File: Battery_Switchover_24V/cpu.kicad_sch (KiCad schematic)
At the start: 42 parts, among them J8 USB_C_Receptacle_USB2.0_14P, SW1 SW_Push, U3 LPC11U14FBD48-201, U4 L5973D, U6 AMS1117-3.3, Y1 12.000MHz

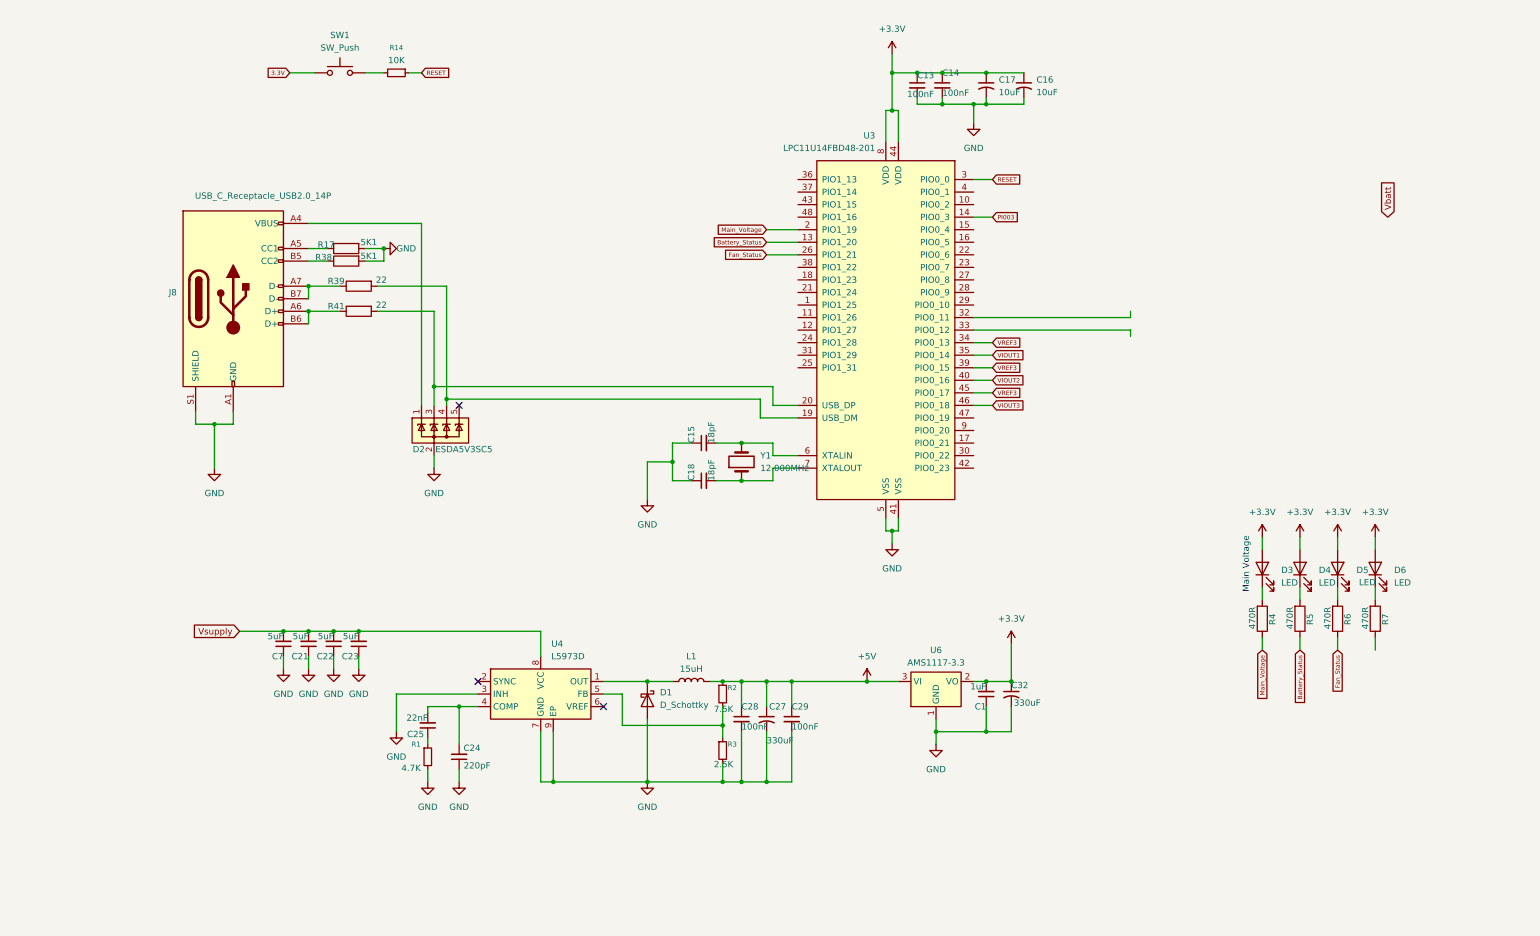
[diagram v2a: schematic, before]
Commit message: Added SCL and SDA from the tempreture sensor to the CPU
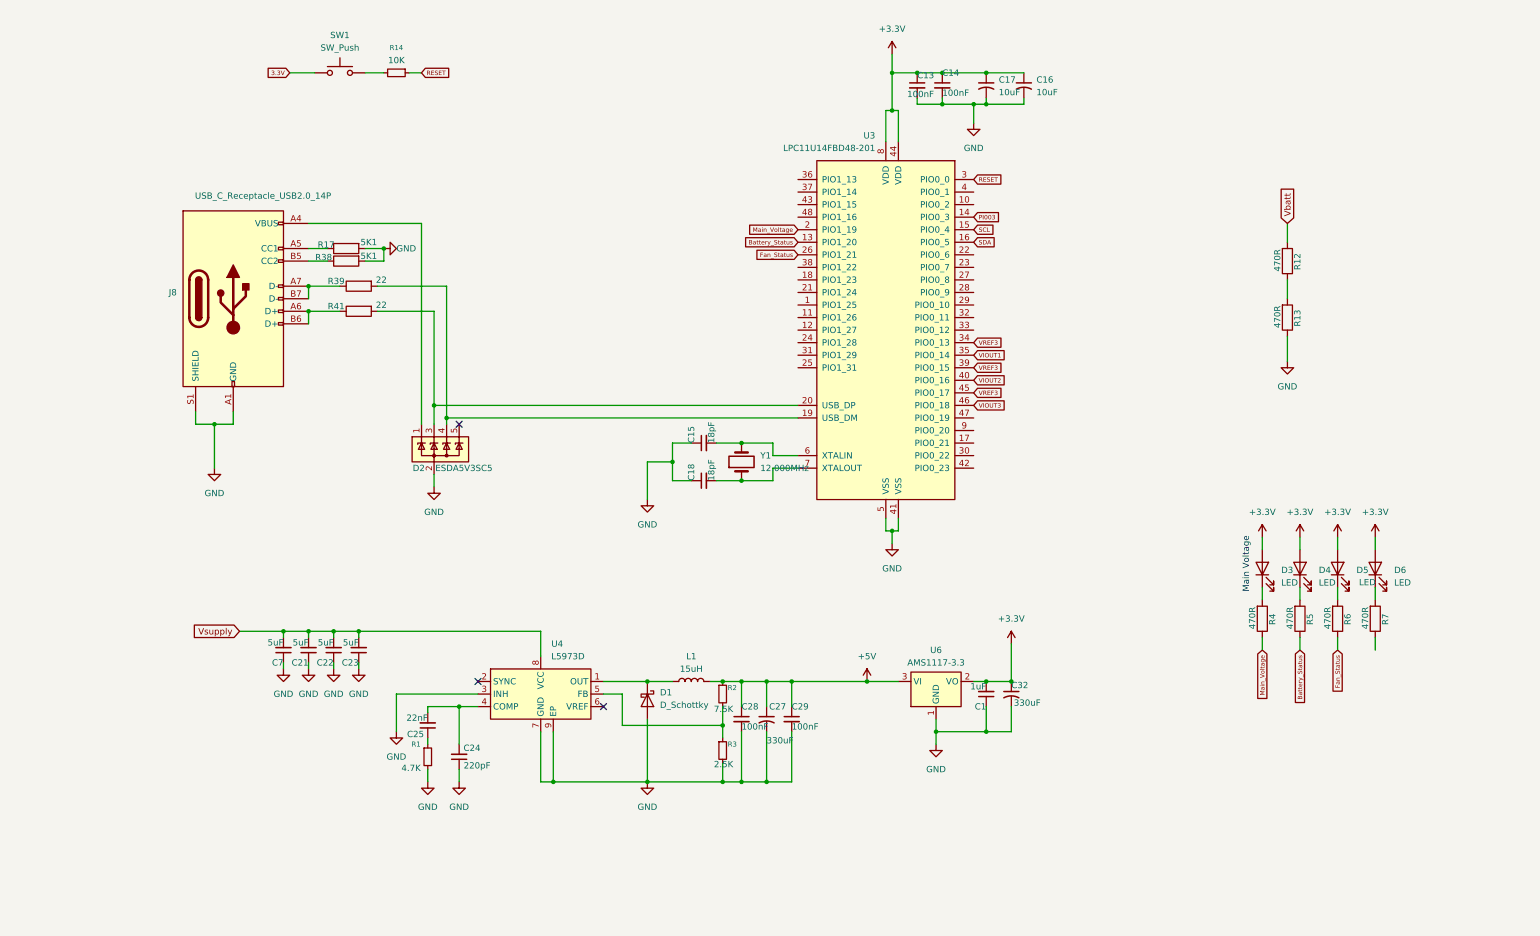
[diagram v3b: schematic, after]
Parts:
- added R12, R13: 470R, Resistor_SMD:R_0603_1608Metric, symbol Device:R
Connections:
- net GND: now also R13.1
- net Vbatt: now also R12.2
- net SCL: now reaches U3.15 (PIO0_4)
- net SDA: now reaches U3.16 (PIO0_5)
- new net: R12.1, R13.2
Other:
- moved on the sheet: C21, C22, C23, C7, D2

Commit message: Voltaj ölçümü eklendi Lm75 LM60 ile değiştirildi
LM75 LM60 ile değiştirildi Vin ve Vbattery voltaj ölçümü için TVS li voltaj bölücüler ADC ye bağlandı Vin 5V converter arasına TVS konuldu 5V converter giriş cap ları değiştirildi. Reset düğmesine debounce cap eklendi.
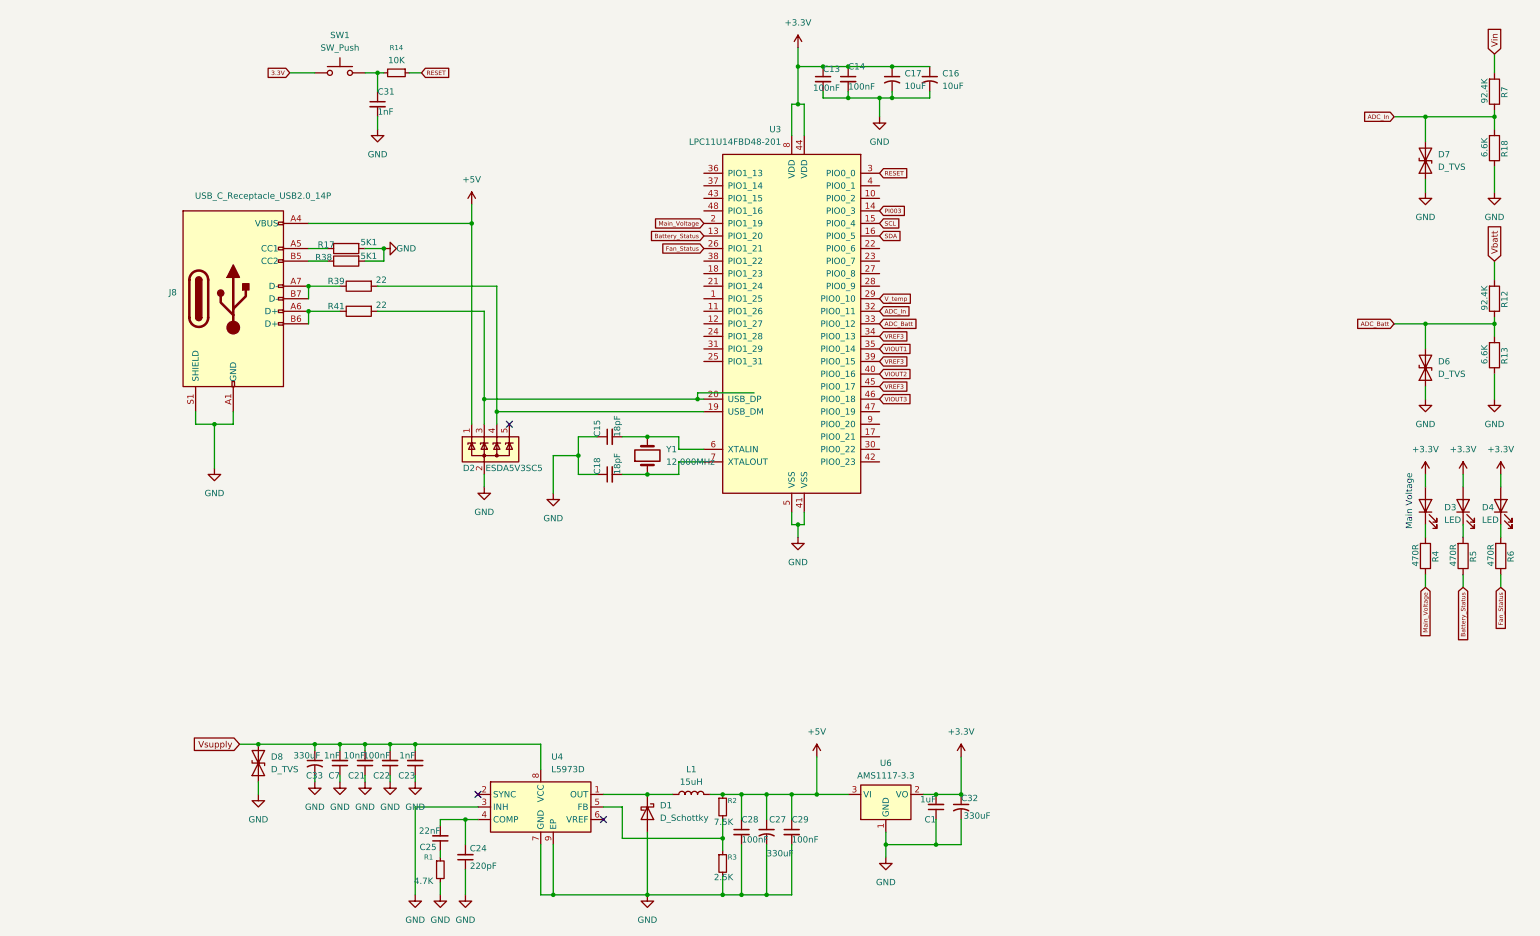
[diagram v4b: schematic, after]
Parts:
- removed D6: LED, symbol Device:LED
- added C31: 1nF, symbol Device:C_Small
- added C33: 330uF, symbol Device:C_Small_US
- added D6, D7, D8: D_TVS, symbol Device:D_TVS
- added R18: 6.6K, Resistor_SMD:R_0603_1608Metric, symbol Device:R
- C21: value 5uF -> 10nF
- C22: value 5uF -> 100nF
- C23, C7: value 5uF -> 1nF
- R12, R7: value 470R -> 92.4K
- R13: value 470R -> 6.6K
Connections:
- net +5V: now also D2.1 (K), J8.A4 (VBUS), J8.A9 (VBUS), J8.B4 (VBUS), J8.B9 (VBUS)
- net GND: now also C31.2, C33.2, D6.1 (A1), D7.1 (A1), D8.1 (A1), R18.1
- net Vsupply: now also C33.1, D8.2 (A2)
- net V_temp: now reaches U3.29 (PIO0_10)
- net ADC_In: now reaches U3.32 (PIO0_11)
- net ADC_In: now also R7.1, D7.2 (A2), R18.2
- net ADC_Batt: now reaches U3.33 (PIO0_12)
- net ADC_Batt: now also R12.1, R13.2, D6.2 (A2)
- net Vin: now reaches R7.2
- net at R14.2, SW1.2: now also C31.1
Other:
- moved on the sheet: C1, C13, C14, C15, C16, C17, C18, C21, C22, C23, C24, C25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

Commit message: Added Some Protection MEasures and redid the Fan Contrlll
Added TVS diodes battery monitor inputs and outputs and some capacitors added fan controll fixed output capacitances of battery monitoring circuit
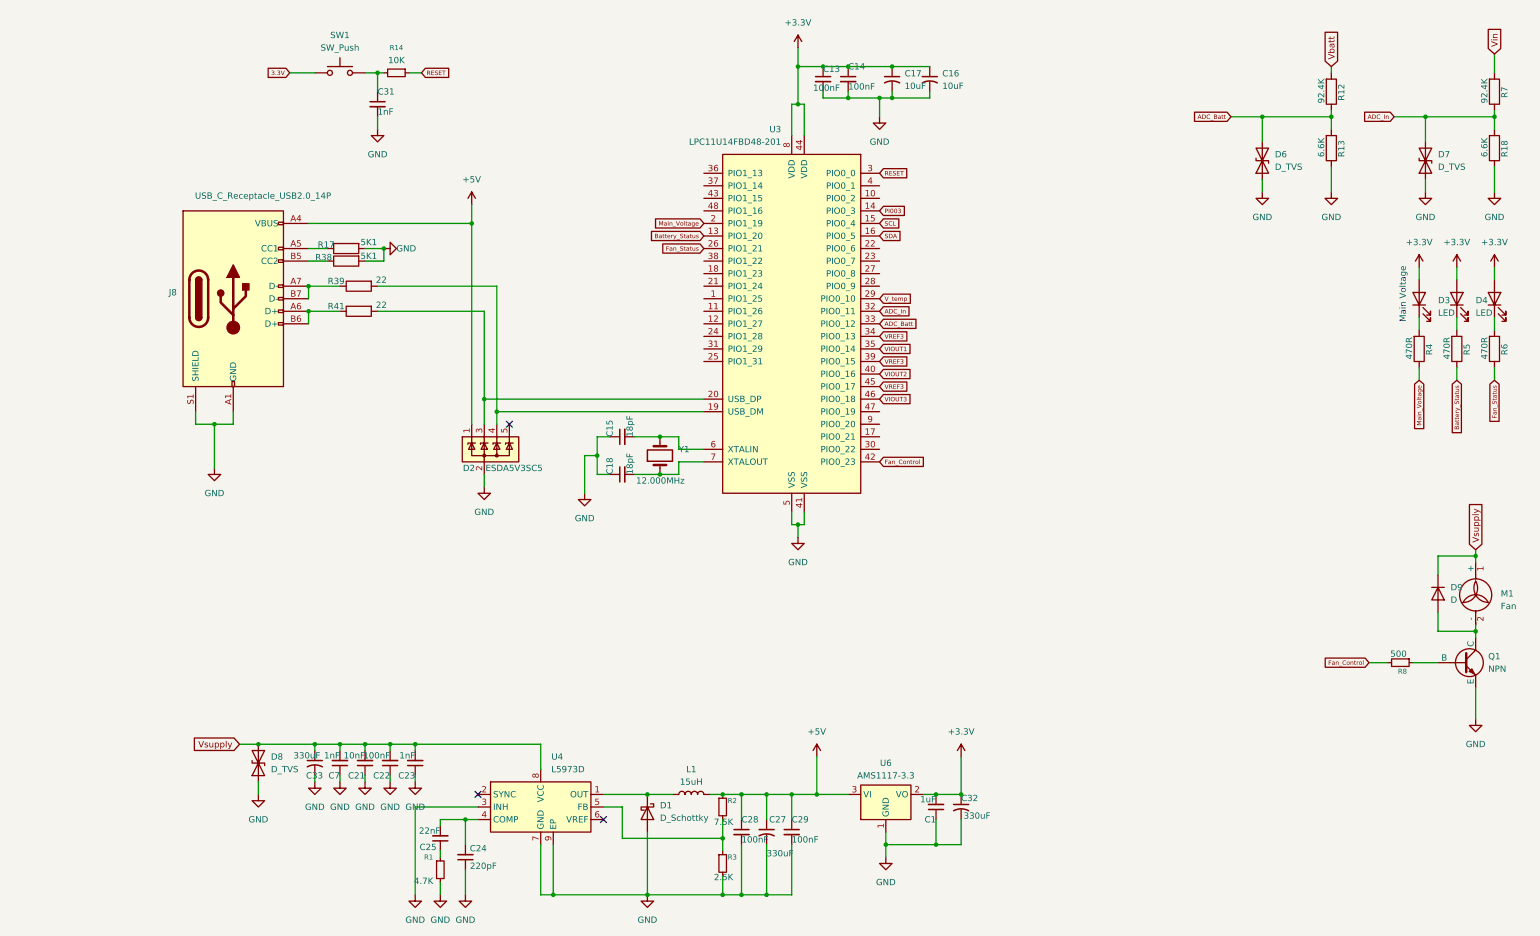
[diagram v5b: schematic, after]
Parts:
- added D9: D, symbol Device:D
- added M1: Fan, symbol Motor:Fan
- added Q1: NPN, symbol Simulation_SPICE:NPN
- added R8: 500, symbol Device:R_Small
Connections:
- net GND: now also Q1.3 (E)
- net Vsupply: now also D9.1 (K), M1.1 (+)
- net Fan_Control: now reaches U3.42 (PIO0_23)
- net Fan_Control: now also R8.2
- new net: D9.2 (A), M1.2 (-), Q1.1 (C)
- new net: Q1.2 (B), R8.1
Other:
- moved on the sheet: C15, C18, D3, D4, D6, R12, R13, R4, R5, R6, Y1

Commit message: Added some Model Numbers For TVS diodes
Added TVS diode model for ADC and
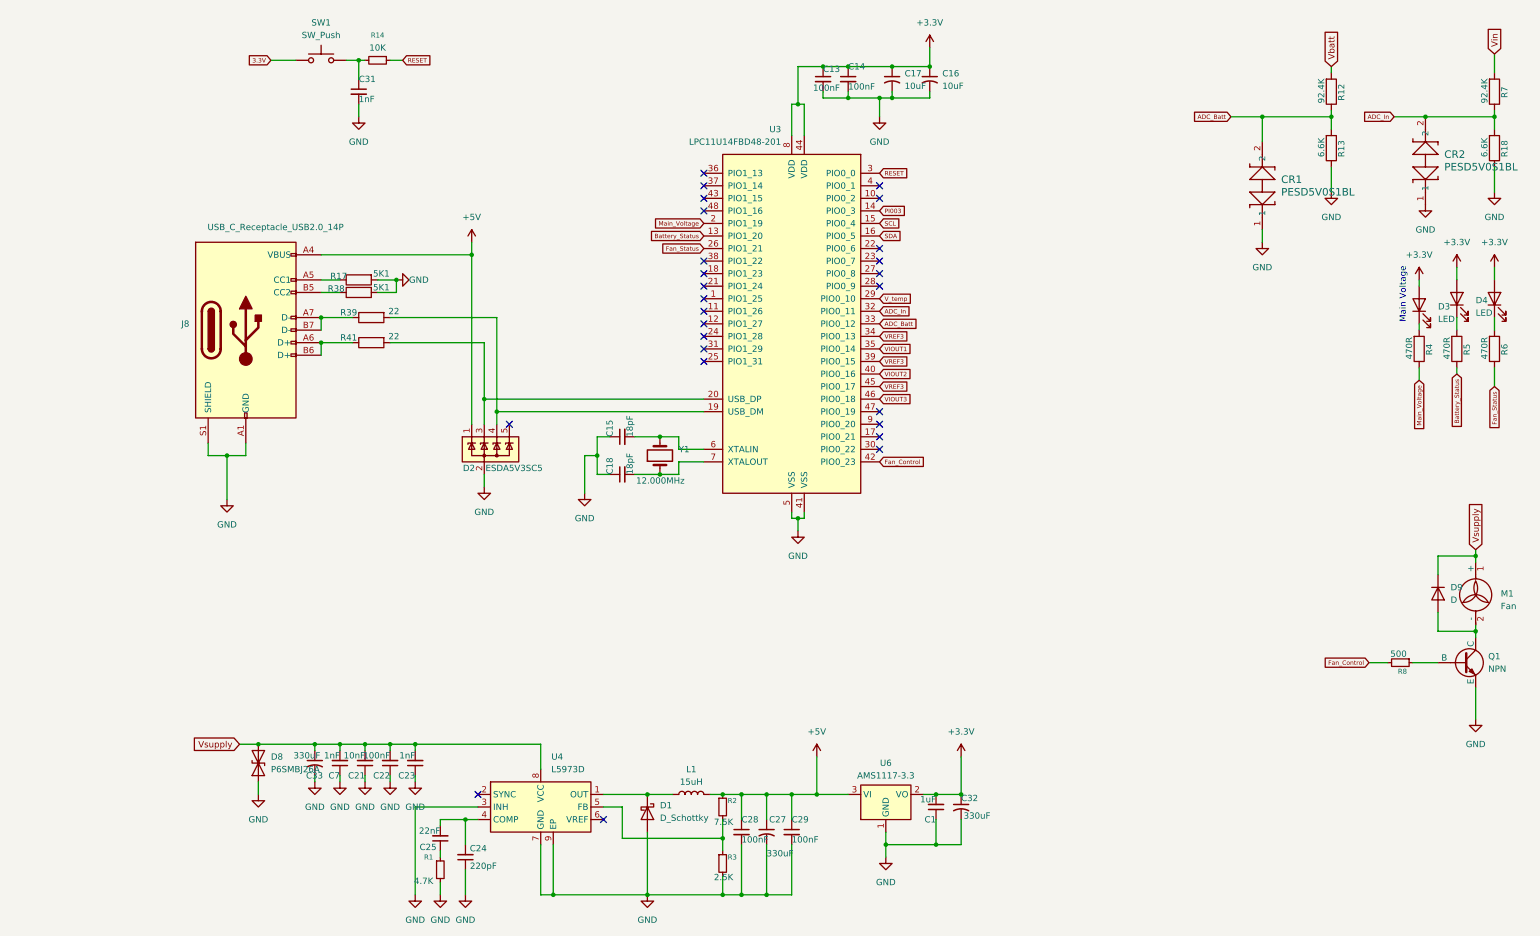
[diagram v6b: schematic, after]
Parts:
- removed D6, D7: D_TVS, symbol Device:D_TVS
- added CR1, CR2: PESD5V0S1BL, SOD882_NXP, symbol PESD5V0S1BL:PESD5V0S1BL
- D8: value D_TVS -> P6SMBJ26A
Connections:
- net ADC_Batt: now also CR1.2
- net ADC_In: now also CR2.2
- net GND: now also CR1.1, CR2.1
- no-connect marks 3 -> 26
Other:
- moved on the sheet: C31, D3, J8, R14, R17, R38, R39, R41, SW1

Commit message: Added CM filter
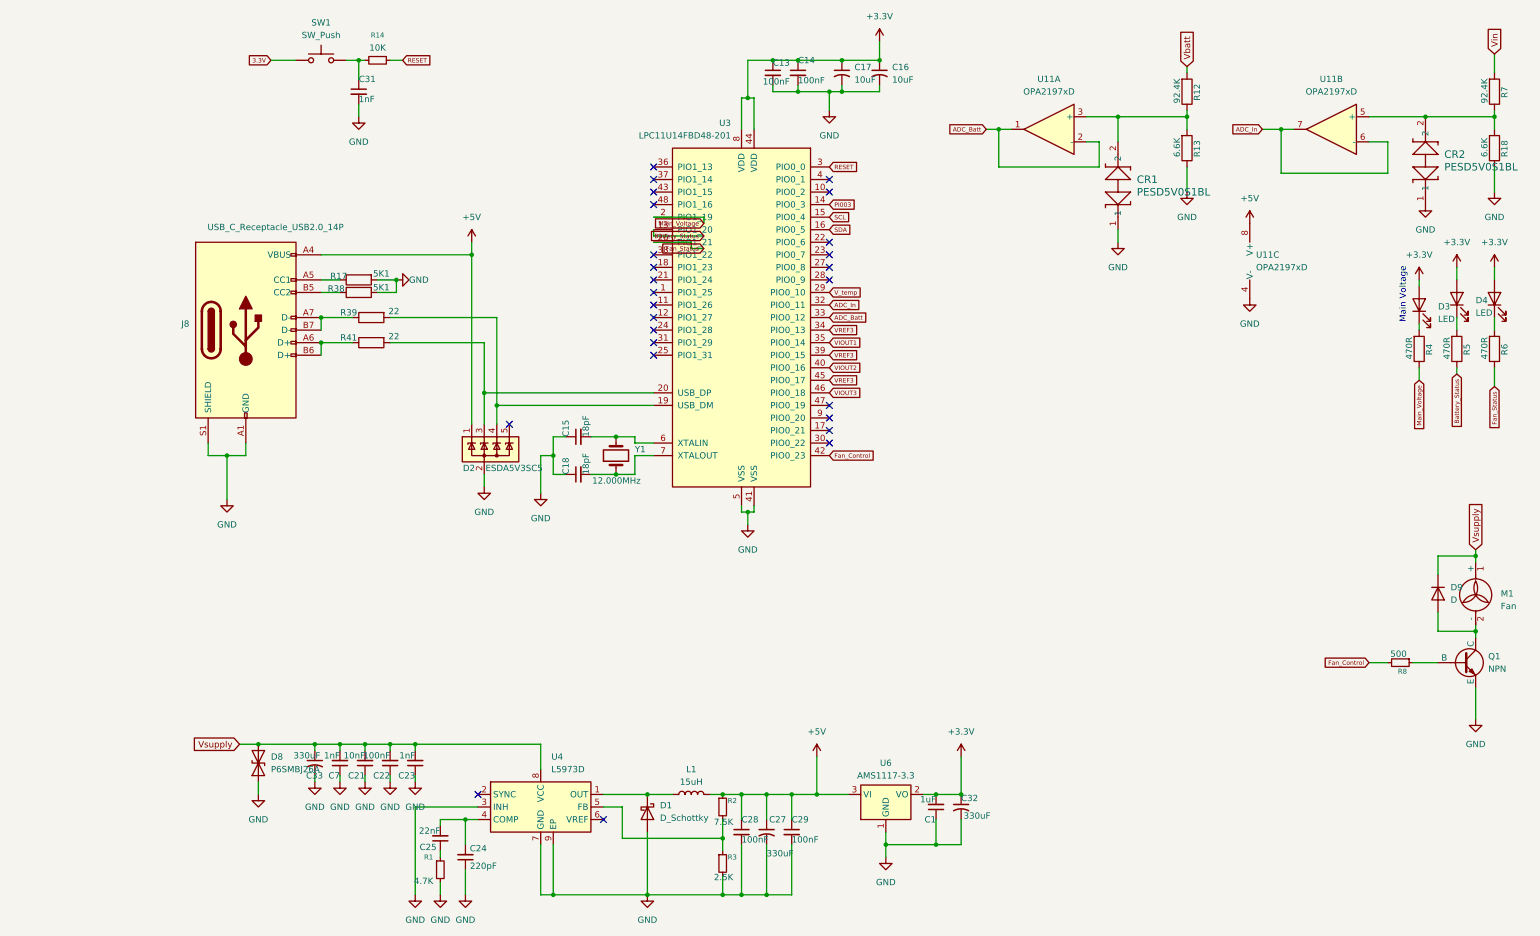
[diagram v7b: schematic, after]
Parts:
- added U11: OPA2197xD, Package_SO:SOIC-8_3.9x4.9mm_P1.27mm, symbol Amplifier_Operational:OPA2197xD
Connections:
- net +5V: now also U11.8 (V+)
- net ADC_Batt: now also U11.1, U11.2 (-); no longer CR1.2, R12.1, R13.2
- net ADC_In: now also U11.6 (-), U11.7; no longer CR2.2, R18.2, R7.1
- net GND: now also U11.4 (V-)
- new net: CR2.2, R18.2, R7.1, U11.5 (+)
- new net: CR1.2, R12.1, R13.2, U11.3 (+)
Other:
- moved on the sheet: C13, C14, C15, C16, C17, C18, CR1, R12, R13, U3, Y1
